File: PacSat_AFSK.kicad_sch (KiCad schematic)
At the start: 4 parts

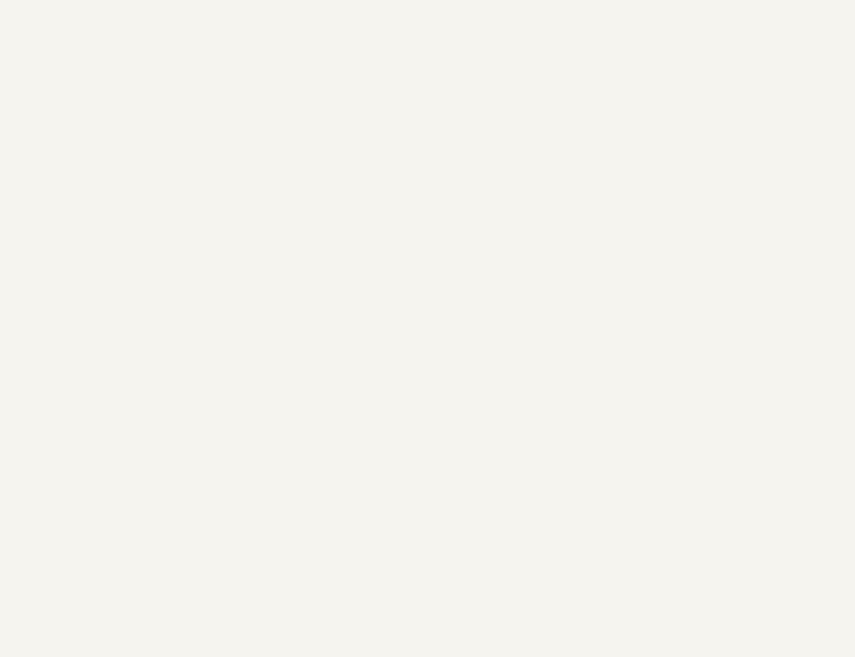
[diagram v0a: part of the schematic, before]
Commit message: Add fiducials for the board house
1mm square and 1mm round fiducials on 3 corners of the board, per
the board house specification.

Signed-off-by: Corey Minyard <corey@minyard.net>
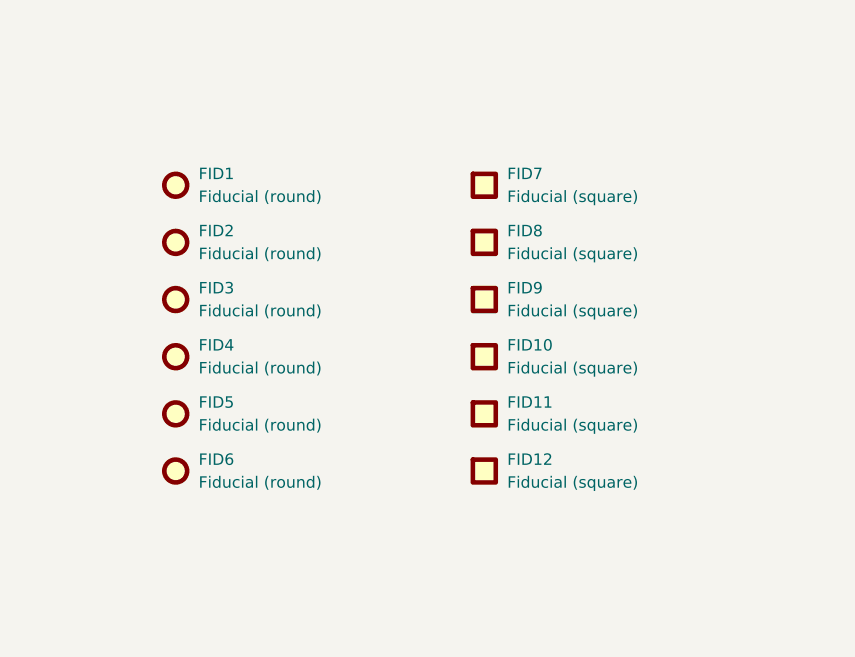
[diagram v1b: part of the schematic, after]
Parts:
- added FID1, FID2, FID3, FID4, FID5, FID6: Fiducial (round), Fiducial:Fiducial_1mm_Mask2mm, symbol Mechanical:Fiducial
- added FID10, FID11, FID12, FID7, FID8, FID9: Fiducial (square), PacSatDev_misc:Fiducial_Square_1mm_Mask2mm, symbol PACSAT_DEV_misc:Fiducial (square)

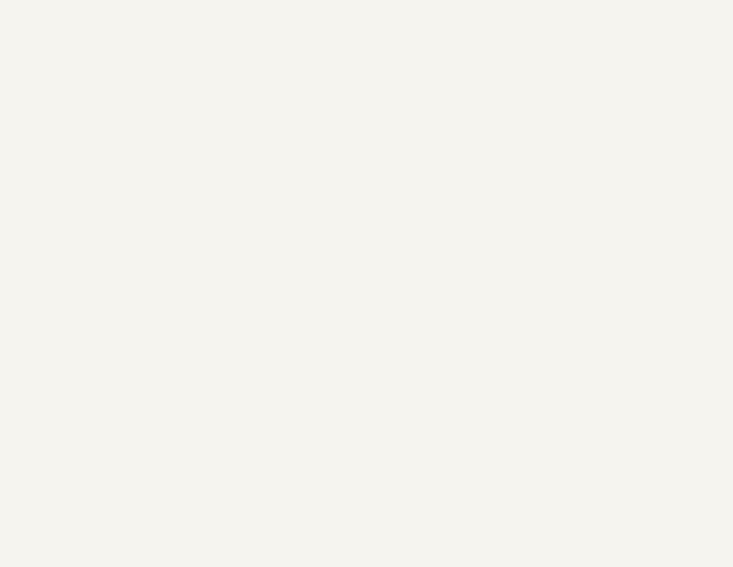
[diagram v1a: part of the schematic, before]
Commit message: Add strain relief for cabling options for the antenna connector
Signed-off-by: Corey Minyard <corey@minyard.net>
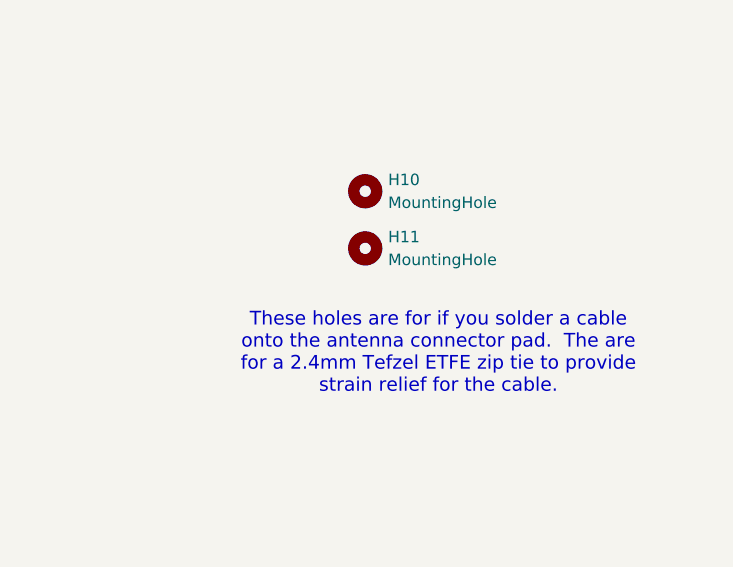
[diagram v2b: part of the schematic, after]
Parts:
- added H10, H11: MountingHole, MountingHole:MountingHole_2.7mm, symbol Mechanical:MountingHole
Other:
- note added: "These holes are for if you solder a cable onto the antenna connector pad. The are for a 2.4mm Tefzel ETFE zip tie to provide strain relief for the cable."
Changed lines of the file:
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@@
 		(comment 1 "N5BRG")
+	)
+	(text "These holes are for if you solder a cable\nonto the antenna connector pad.  The are\nfor a 2.4mm Tefzel ETFE zip tie to provide\nstrain relief for the cable."
+		(exclude_from_sim no)
+		(at 237.998 218.694 0)
+		(effects
+			(font
+				(size 1.524 1.524)
+			)
+		)
 	)
 	(junction
@@
 	)
 	(symbol
+		(lib_id "Mechanical:MountingHole")
+		(at 229.87 200.66 0)
+		(unit 1)
+		(exclude_from_sim no)
+		(in_bom no)
+		(on_board yes)
+		(dnp no)
+		(fields_autoplaced yes)
+		(property "Reference" "H10"
+			(at 232.41 199.3899 0)
+			(effects
+				(font
+					(size 1.27 1.27)
+				)
+				(justify left)
+			)
+		)
+		(property "Value" "MountingHole"
+			(at 232.41 201.9299 0)
+			(effects
+				(font
+					(size 1.27 1.27)
+				)
+				(justify left)
+			)
+		)
+		(property "Footprint" "MountingHole:MountingHole_2.7mm"
+			(at 229.87 200.66 0)
+			(effects
+				(font
+					(size 1.27 1.27)
+				)
+				(hide yes)
+			)
+		)
+		(property "Datasheet" "~"
+			(at 229.87 200.66 0)
+			(effects
+				(font
+					(size 1.27 1.27)
+				)
+				(hide yes)
+			)
+		)
+		(property "Description" "Mounting Hole without connection"
+			(at 229.87 200.66 0)
+			(effects
+				(font
+					(size 1.27 1.27)
+				)
+				(hide yes)
+			)
+		)
+		(instances
+			(project ""
+				(path "/cc9f42d2-6985-41ac-acab-5ab7b01c5b38"
+					(reference "H10")
+					(unit 1)
+				)
+			)
+		)
+	)
+	(symbol
 		(lib_id "Mechanical:Fiducial")
 		(at 93.98 204.47 0)
@@
 					(unit 1)
 				)
+			)
+		)
+	)
+	(symbol
+		(lib_id "Mechanical:MountingHole")
+		(at 229.87 207.01 0)
+		(unit 1)
+		(exclude_from_sim no)
+		(in_bom no)
+		(on_board yes)
+		(dnp no)
+		(fields_autoplaced yes)
+		(property "Reference" "H11"
+			(at 232.41 205.7399 0)
+			(effects
+				(font
+					(size 1.27 1.27)
+				)
+				(justify left)
+			)
+		)
+		(property "Value" "MountingHole"
+			(at 232.41 208.2799 0)
+			(effects
+				(font
+					(size 1.27 1.27)
+				)
+				(justify left)
+			)
+		)
+		(property "Footprint" "MountingHole:MountingHole_2.7mm"
+			(at 229.87 207.01 0)
+			(effects
+				(font
+					(size 1.27 1.27)
+				)
+				(hide yes)
+			)
+		)
+		(property "Datasheet" "~"
+			(at 229.87 207.01 0)
+			(effects
+				(font
+					(size 1.27 1.27)
+				)
+				(hide yes)
+			)
+		)
+		(property "Description" "Mounting Hole without connection"
+			(at 229.87 207.01 0)
+			(effects
+				(font
+					(size 1.27 1.27)
+				)
+				(hide yes)
+			)
+		)
+		(instances
+			(project "PacSat_AFSK"
+				(path "/cc9f42d2-6985-41ac-acab-5ab7b01c5b38"
+					(reference "H11")
+					(unit 1)
+				)

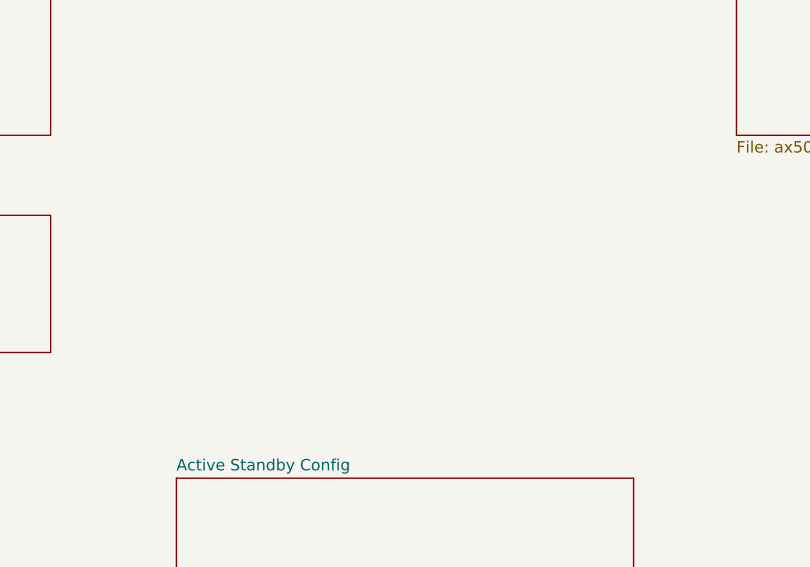
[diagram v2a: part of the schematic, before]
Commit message: Add a connection for an external antenna controller
Remove the SPI connection to the PC104 and use it for a SPI to I2C
converter microprocessor.  Add a connector for the external antenna
controller.

Signed-off-by: Corey Minyard <corey@minyard.net>
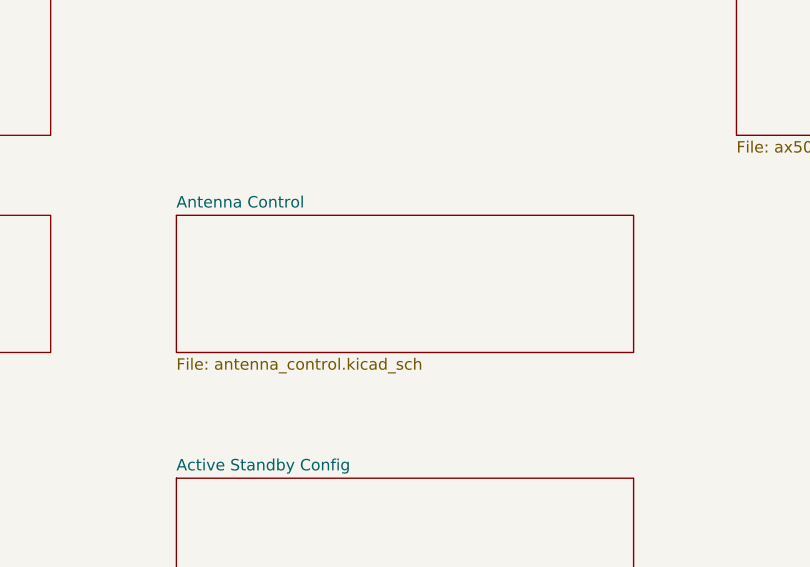
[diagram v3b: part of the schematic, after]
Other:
- added sheet Antenna Control (antenna_control.kicad_sch)
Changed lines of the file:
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@@
+	)
+	(sheet
+		(at 113.03 97.79)
+		(size 50.8 15.24)
+		(exclude_from_sim no)
+		(in_bom yes)
+		(on_board yes)
+		(dnp no)
+		(fields_autoplaced yes)
+		(stroke
+			(width 0.1524)
+			(type solid)
+		)
+		(fill
+			(color 0 0 0 0.0000)
+		)
+		(property "Sheetname" "Antenna Control"
+			(at 113.03 97.0784 0)
+			(effects
+				(font
+					(size 1.27 1.27)
+				)
+				(justify left bottom)
+			)
+		)
+		(property "Sheetfile" "antenna_control.kicad_sch"
+			(at 113.03 113.6146 0)
+			(effects
+				(font
+					(size 1.27 1.27)
+				)
+				(justify left top)
+			)
+		)
+		(property "Field2" ""
+			(at 113.03 97.79 0)
+			(effects
+				(font
+					(size 1.27 1.27)
+				)
+			)
+		)
+		(instances
+			(project "PacSat_AFSK"
+				(path "/cc9f42d2-6985-41ac-acab-5ab7b01c5b38"
+					(page "20")
+				)
+			)
+		)
 	)
 	(sheet

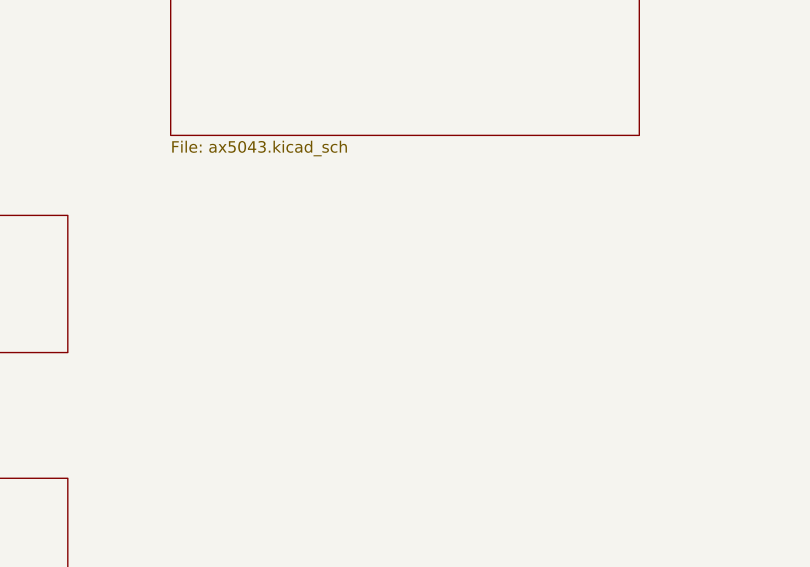
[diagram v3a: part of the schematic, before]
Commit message: Add a USB serial and power interface to the board
Signed-off-by: Corey Minyard <corey@minyard.net>
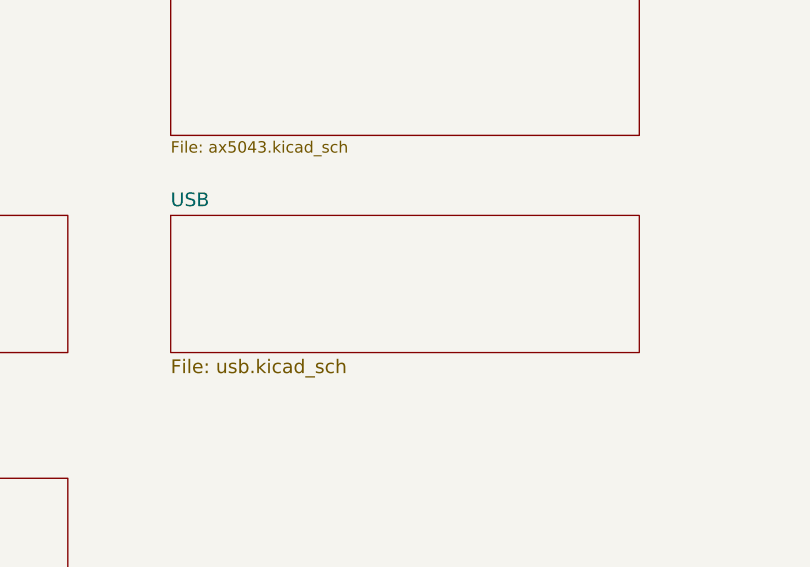
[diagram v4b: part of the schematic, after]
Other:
- added sheet USB (usb.kicad_sch)
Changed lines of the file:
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@@
+		)
+	)
+	(sheet
+		(at 175.26 97.79)
+		(size 52.07 15.24)
+		(exclude_from_sim no)
+		(in_bom yes)
+		(on_board yes)
+		(dnp no)
+		(fields_autoplaced yes)
+		(stroke
+			(width 0)
+			(type solid)
+		)
+		(fill
+			(color 0 0 0 0.0000)
+		)
+		(property "Sheetname" "USB"
+			(at 175.26 96.9514 0)
+			(effects
+				(font
+					(size 1.524 1.524)
+				)
+				(justify left bottom)
+			)
+		)
+		(property "Sheetfile" "usb.kicad_sch"
+			(at 175.26 113.7162 0)
+			(effects
+				(font
+					(size 1.524 1.524)
+				)
+				(justify left top)
+			)
+		)
+		(instances
+			(project "PacSat_AFSK"
+				(path "/cc9f42d2-6985-41ac-acab-5ab7b01c5b38"
+					(page "22")
+				)
+			)
 		)
 	)
